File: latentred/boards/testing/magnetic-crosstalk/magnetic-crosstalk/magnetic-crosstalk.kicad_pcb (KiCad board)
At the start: 4 copper layers, 82.4 x 89 mm, 45 parts, among them J1 STEWART_SS_74500_024, J2 SMA, J3 SMA, J4 SMA, J5 SMA, J6 SMA, J7 SMA, J8 SMA, J9 SMA

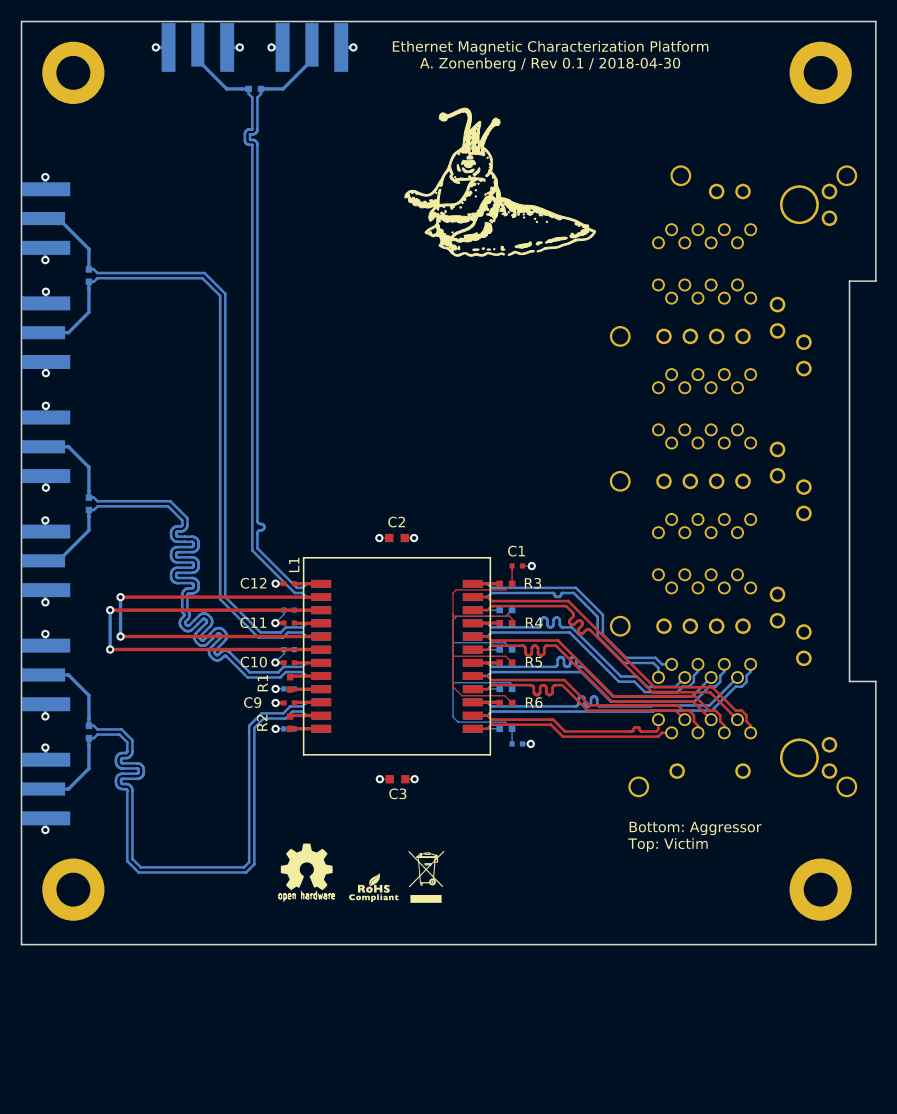
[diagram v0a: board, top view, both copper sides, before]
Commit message: Finished initial version of crosstalk characterization board
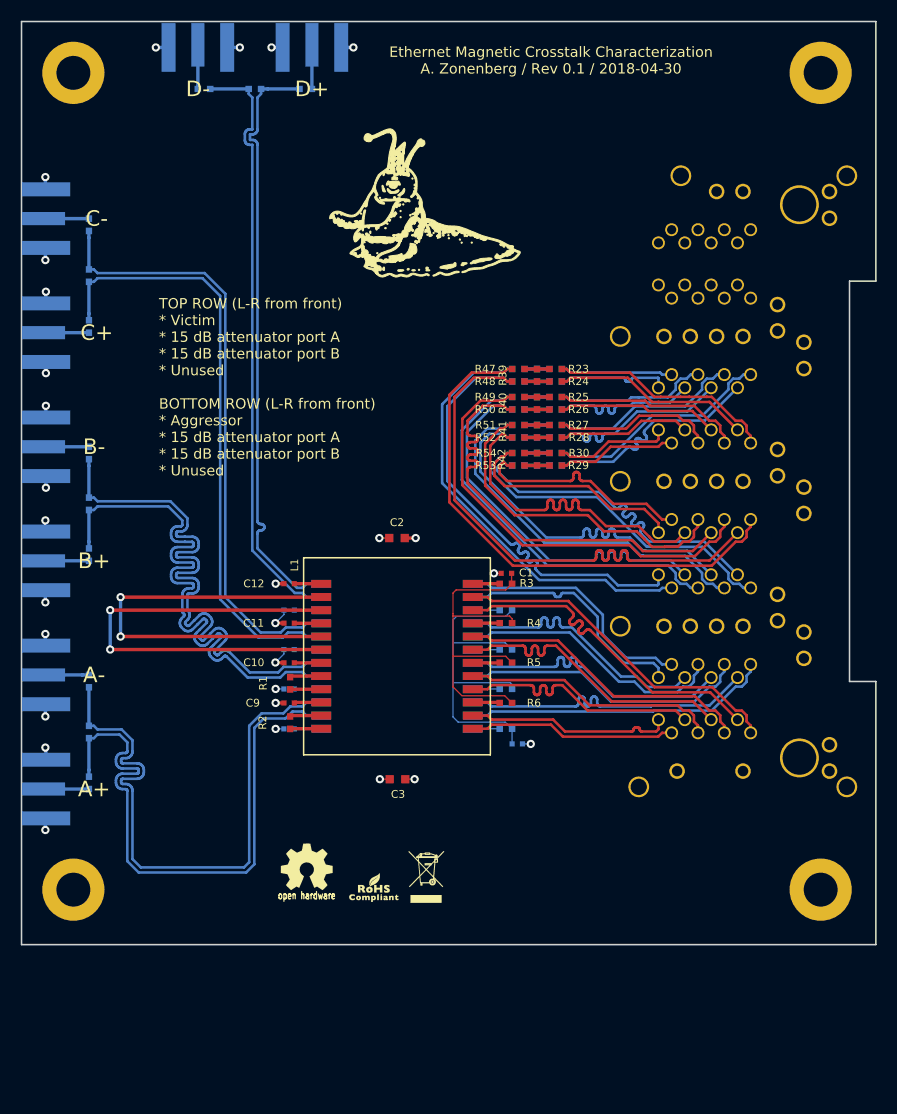
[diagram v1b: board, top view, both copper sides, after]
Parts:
- added R15: 953, azonenberg_pcb:EIA_0402_RES_NOSILK, B.Cu at (171.5, 94.4)
- added R16: 953, azonenberg_pcb:EIA_0402_RES_NOSILK, B.Cu at (171.5, 84.6)
- added R17: 953, azonenberg_pcb:EIA_0402_RES_NOSILK, B.Cu at (171.5, 72.4)
- added R18: 953, azonenberg_pcb:EIA_0402_RES_NOSILK, B.Cu at (171.5, 62.6)
- added R19: 953, azonenberg_pcb:EIA_0402_RES_NOSILK, B.Cu at (171.5, 50.4)
- added R20: 953, azonenberg_pcb:EIA_0402_RES_NOSILK, B.Cu at (171.5, 40.6)
- added R21: 953, azonenberg_pcb:EIA_0402_RES_NOSILK, B.Cu at (192.4, 27.5)
- added R22: 953, azonenberg_pcb:EIA_0402_RES_NOSILK, B.Cu at (182.6, 27.5)
- added R23: 34.8, azonenberg_pcb:EIA_0402_RES_NOSILK, F.Cu at (216.5, 54.5)
- added R24: 34.8, azonenberg_pcb:EIA_0402_RES_NOSILK, F.Cu at (216.5, 55.7)
- added R25: 34.8, azonenberg_pcb:EIA_0402_RES_NOSILK, F.Cu at (216.5, 57.2)
- added R26: 34.8, azonenberg_pcb:EIA_0402_RES_NOSILK, F.Cu at (216.5, 58.4)
- added R27: 34.8, azonenberg_pcb:EIA_0402_RES_NOSILK, F.Cu at (216.5, 59.9)
- added R28: 34.8, azonenberg_pcb:EIA_0402_RES_NOSILK, F.Cu at (216.5, 61.1)
- added R29: 34.8, azonenberg_pcb:EIA_0402_RES_NOSILK, F.Cu at (216.5, 63.8)
- added R30: 34.8, azonenberg_pcb:EIA_0402_RES_NOSILK, F.Cu at (216.5, 62.6)
- added R31: 34.8, azonenberg_pcb:EIA_0402_RES_NOSILK, B.Cu at (212.9, 62.6)
- added R32: 34.8, azonenberg_pcb:EIA_0402_RES_NOSILK, B.Cu at (212.9, 63.8)
- added R33: 34.8, azonenberg_pcb:EIA_0402_RES_NOSILK, B.Cu at (212.9, 59.9)
- added R34: 34.8, azonenberg_pcb:EIA_0402_RES_NOSILK, B.Cu at (212.9, 61.1)
- added R35: 34.8, azonenberg_pcb:EIA_0402_RES_NOSILK, B.Cu at (212.9, 57.2)
- added R36: 34.8, azonenberg_pcb:EIA_0402_RES_NOSILK, B.Cu at (212.9, 58.4)
- added R37: 34.8, azonenberg_pcb:EIA_0402_RES_NOSILK, B.Cu at (212.9, 54.5)
- added R38: 34.8, azonenberg_pcb:EIA_0402_RES_NOSILK, B.Cu at (212.9, 55.7)
- added R39: 36.5, azonenberg_pcb:EIA_0402_RES_NOSILK, F.Cu at (214.7, 55.1)
- added R40: 36.5, azonenberg_pcb:EIA_0402_RES_NOSILK, F.Cu at (214.7, 57.8)
- added R41: 36.5, azonenberg_pcb:EIA_0402_RES_NOSILK, F.Cu at (214.7, 60.5)
- added R42: 36.5, azonenberg_pcb:EIA_0402_RES_NOSILK, F.Cu at (214.7, 63.2)
- added R43: 36.5, azonenberg_pcb:EIA_0402_RES_NOSILK, B.Cu at (214.7, 63.2)
- added R44: 36.5, azonenberg_pcb:EIA_0402_RES_NOSILK, B.Cu at (214.7, 60.5)
- added R45: 36.5, azonenberg_pcb:EIA_0402_RES_NOSILK, B.Cu at (214.7, 57.8)
- added R46: 36.5, azonenberg_pcb:EIA_0402_RES_NOSILK, B.Cu at (214.7, 55.1)
- added R47: 34.8, azonenberg_pcb:EIA_0402_RES_NOSILK, F.Cu at (212.9, 54.5)
- added R48: 34.8, azonenberg_pcb:EIA_0402_RES_NOSILK, F.Cu at (212.9, 55.7)
- added R49: 34.8, azonenberg_pcb:EIA_0402_RES_NOSILK, F.Cu at (212.9, 57.2)
- added R50: 34.8, azonenberg_pcb:EIA_0402_RES_NOSILK, F.Cu at (212.9, 58.4)
- added R51: 34.8, azonenberg_pcb:EIA_0402_RES_NOSILK, F.Cu at (212.9, 59.9)
- added R52: 34.8, azonenberg_pcb:EIA_0402_RES_NOSILK, F.Cu at (212.9, 61.1)
- added R53: 34.8, azonenberg_pcb:EIA_0402_RES_NOSILK, F.Cu at (212.9, 63.8)
- added R54: 34.8, azonenberg_pcb:EIA_0402_RES_NOSILK, F.Cu at (212.9, 62.6)
- added R55: 34.8, azonenberg_pcb:EIA_0402_RES_NOSILK, B.Cu at (216.5, 62.6)
- added R56: 34.8, azonenberg_pcb:EIA_0402_RES_NOSILK, B.Cu at (216.5, 63.8)
- added R57: 34.8, azonenberg_pcb:EIA_0402_RES_NOSILK, B.Cu at (216.5, 59.9)
- added R58: 34.8, azonenberg_pcb:EIA_0402_RES_NOSILK, B.Cu at (216.5, 61.1)
- added R59: 34.8, azonenberg_pcb:EIA_0402_RES_NOSILK, B.Cu at (216.5, 57.2)
- added R60: 34.8, azonenberg_pcb:EIA_0402_RES_NOSILK, B.Cu at (216.5, 58.4)
- added R61: 34.8, azonenberg_pcb:EIA_0402_RES_NOSILK, B.Cu at (216.5, 54.5)
- added R62: 34.8, azonenberg_pcb:EIA_0402_RES_NOSILK, B.Cu at (216.5, 55.7)
- moved G*** 7.52 mm to (205.0, 39.2)
- moved C1 1.26 mm to (211.8, 74.2), turned to 0 degrees
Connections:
- J1 pad C1: (no net) -> /A2_A_P
- J1 pad C10: (no net) -> Net-(J1-PadC10)
- J1 pad C11: (no net) -> Net-(J1-PadC11)
- J1 pad C12: (no net) -> Net-(J1-PadC12)
- J1 pad C2: (no net) -> /A2_A_N
- J1 pad C3: (no net) -> /A2_B_P
- J1 pad C4: (no net) -> /A2_B_N
- J1 pad C5: (no net) -> /A2_C_P
- J1 pad C6: (no net) -> /A2_C_N
- J1 pad C7: (no net) -> /A2_D_P
- J1 pad C8: (no net) -> /A2_D_N
- J1 pad C9: (no net) -> Net-(J1-PadC9)
- J1 pad D1: (no net) -> /A1X_A_P
- J1 pad D10: (no net) -> Net-(J1-PadD10)
- J1 pad D11: (no net) -> Net-(J1-PadD11)
- J1 pad D12: (no net) -> Net-(J1-PadD12)
- J1 pad D2: (no net) -> /A1X_A_N
- J1 pad D3: (no net) -> /A1X_B_P
- J1 pad D4: (no net) -> /A1X_B_N
- J1 pad D5: (no net) -> /A1X_C_P
- J1 pad D6: (no net) -> /A1X_C_N
- J1 pad D7: (no net) -> /A1X_D_P
- J1 pad D8: (no net) -> /A1X_D_N
- J1 pad D9: (no net) -> Net-(J1-PadD9)
- J1 pad E1: (no net) -> /A1_A_P
- J1 pad E10: (no net) -> Net-(J1-PadE10)
- J1 pad E11: (no net) -> Net-(J1-PadE11)
- J1 pad E12: (no net) -> Net-(J1-PadE12)
- J1 pad E2: (no net) -> /A1_A_N
- J1 pad E3: (no net) -> /A1_B_P
- J1 pad E4: (no net) -> /A1_B_N
- J1 pad E5: (no net) -> /A1_C_P
- J1 pad E6: (no net) -> /A1_C_N
- J1 pad E7: (no net) -> /A1_D_P
- J1 pad E8: (no net) -> /A1_D_N
- J1 pad E9: (no net) -> Net-(J1-PadE9)
- J1 pad F1: (no net) -> /A2X_A_P
- J1 pad F10: (no net) -> Net-(J1-PadF10)
- J1 pad F11: (no net) -> Net-(J1-PadF11)
- J1 pad F12: (no net) -> Net-(J1-PadF12)
- J1 pad F2: (no net) -> /A2X_A_N
- J1 pad F3: (no net) -> /A2X_B_P
- J1 pad F4: (no net) -> /A2X_B_N
- J1 pad F5: (no net) -> /A2X_C_P
- J1 pad F6: (no net) -> /A2X_C_N
- J1 pad F7: (no net) -> /A2X_D_P
- J1 pad F8: (no net) -> /A2X_D_N
- J1 pad F9: (no net) -> Net-(J1-PadF9)
- J2 pad 1: /A_P -> Net-(J2-Pad1)
- J3 pad 1: /A_N -> Net-(J3-Pad1)
- J4 pad 1: /B_P -> Net-(J4-Pad1)
- J5 pad 1: /B_N -> Net-(J5-Pad1)
- J6 pad 1: /C_P -> Net-(J6-Pad1)
- J7 pad 1: /C_N -> Net-(J7-Pad1)
- J8 pad 1: /D_P -> Net-(J8-Pad1)
- J9 pad 1: /D_N -> Net-(J9-Pad1)
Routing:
- net /A1X_A_N: track 0.00 -> 51.6 mm
- net /A1X_A_P: track 0.00 -> 51.6 mm
- net /A1X_B_N: track 0.00 -> 42.4 mm
- net /A1X_B_P: track 0.00 -> 42.4 mm
- net /A2_D_N: track 0.00 -> 42.3 mm
- net /A2_D_P: track 0.00 -> 42.3 mm
- net /A2_C_N: track 0.00 -> 38.4 mm
- net /A2_C_P: track 0.00 -> 38.4 mm
- net /A2_B_N: track 0.00 -> 36.3 mm
- net /A2_B_P: track 0.00 -> 36.3 mm
- net /A2_A_N: track 0.00 -> 33.1 mm
- net /A2_A_P: track 0.00 -> 33.1 mm
- net /A1X_C_N: track 0.00 -> 32.2 mm
- net /A1X_C_P: track 0.00 -> 32.2 mm
- net /GND: track 192.7 -> 219.7 mm
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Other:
- board text added: "A+"
- board text added: "A-"
- board text added: "B+"
- board text added: "B-"
- board text added: "C+"
- board text added: "C-"
- board text added: "D+"
- board text added: "D-"
- board text added: "Ethernet Magnetic Crosstalk Characterization A. Zonenberg / Rev 0.1 / 2018-04-30"
- board text added: "TOP ROW (L-R from front) * Victim * 15 dB attenuator port A * 15 dB attenuator port B * Unused BOTTOM ROW (L-R from front) * Aggressor * 15 dB attenuator port A * 15 dB attenuator port B * Unused"
- board text removed: "Bottom: Aggressor Top: Victim"
- board text removed: "Ethernet Magnetic Characterization Platform A. Zonenberg / Rev 0.1 / 2018-04-30"

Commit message: Began updating magnetic-crosstalk board for v0.2
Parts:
- moved L1 39.9 mm to (228.0, 111.8)
- moved L2 34.8 mm to (201.8, 117.0)
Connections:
- L1 pad 1: Net-(C12-Pad2) -> Net-(L1-Pad1)
- L1 pad 10: Net-(C9-Pad2) -> Net-(L1-Pad10)
- L1 pad 11: Net-(L1-Pad11) -> /AGG_D_N
- L1 pad 12: Net-(L1-Pad12) -> /AGG_D_P
- L1 pad 13: /AGG_D_P -> Net-(L1-Pad13)
- L1 pad 14: /AGG_D_N -> Net-(L1-Pad14)
- L1 pad 15: Net-(L1-Pad15) -> Net-(C9-Pad2)
- L1 pad 16: /AGG_C_N -> Net-(L1-Pad16)
- L1 pad 17: /AGG_C_P -> Net-(L1-Pad17)
- L1 pad 18: Net-(L1-Pad18) -> Net-(C10-Pad2)
- L1 pad 19: /AGG_B_N -> Net-(L1-Pad19)
- L1 pad 2: Net-(L1-Pad2) -> /AGG_A_P
- L1 pad 20: /AGG_B_P -> Net-(L1-Pad20)
- L1 pad 21: Net-(L1-Pad21) -> Net-(C11-Pad2)
- L1 pad 22: /AGG_A_N -> Net-(L1-Pad19)
- L1 pad 23: /AGG_A_P -> Net-(L1-Pad20)
- L1 pad 24: Net-(L1-Pad24) -> Net-(C12-Pad2)
- L1 pad 3: Net-(L1-Pad3) -> /AGG_A_N
- L1 pad 4: Net-(C11-Pad2) -> Net-(L1-Pad4)
- L1 pad 5: Net-(L1-Pad2) -> /AGG_B_P
- L1 pad 6: Net-(L1-Pad3) -> /AGG_B_N
- L1 pad 7: Net-(C10-Pad2) -> Net-(L1-Pad7)
- L1 pad 8: Net-(L1-Pad8) -> /AGG_C_P
- L1 pad 9: Net-(L1-Pad9) -> /AGG_C_N
- L2 pad 1: Net-(C7-Pad2) -> Net-(L2-Pad1)
- L2 pad 10: Net-(C4-Pad2) -> Net-(L2-Pad10)
- L2 pad 11: /D_N -> /VIC_D_N
- L2 pad 12: /D_P -> /VIC_D_P
- L2 pad 13: /VIC_D_P -> /D_P
- L2 pad 14: /VIC_D_N -> /D_N
- L2 pad 15: Net-(L2-Pad15) -> Net-(C4-Pad2)
- L2 pad 16: /VIC_C_N -> /C_N
- L2 pad 17: /VIC_C_P -> /C_P
- L2 pad 18: Net-(L2-Pad18) -> Net-(C5-Pad2)
- L2 pad 19: /VIC_B_N -> /B_N
- L2 pad 2: /A_P -> /VIC_A_P
- L2 pad 20: /VIC_B_P -> /B_P
- L2 pad 21: Net-(L2-Pad21) -> Net-(C6-Pad2)
- L2 pad 22: /VIC_A_N -> /A_N
- L2 pad 23: /VIC_A_P -> /A_P
- L2 pad 24: Net-(L2-Pad24) -> Net-(C7-Pad2)
- L2 pad 3: /A_N -> /VIC_A_N
- L2 pad 4: Net-(C6-Pad2) -> Net-(L2-Pad4)
- L2 pad 5: /B_P -> /VIC_B_P
- L2 pad 6: /B_N -> /VIC_B_N
- L2 pad 7: Net-(C5-Pad2) -> Net-(L2-Pad7)
- L2 pad 8: /C_P -> /VIC_C_P
- L2 pad 9: /C_N -> /VIC_C_N
- R1 pad 1: Net-(L1-Pad8) -> Net-(L1-Pad17)
- R1 pad 2: Net-(L1-Pad9) -> Net-(L1-Pad16)
- R11 pad 2: Net-(L2-Pad24) -> Net-(L2-Pad1)
- R12 pad 2: Net-(L2-Pad21) -> Net-(L2-Pad4)
- R13 pad 2: Net-(L2-Pad18) -> Net-(L2-Pad7)
- R14 pad 2: Net-(L2-Pad15) -> Net-(L2-Pad10)
- R2 pad 1: Net-(L1-Pad11) -> Net-(L1-Pad14)
- R2 pad 2: Net-(L1-Pad12) -> Net-(L1-Pad13)
- R3 pad 2: Net-(L1-Pad24) -> Net-(L1-Pad1)
- R4 pad 2: Net-(L1-Pad21) -> Net-(L1-Pad4)
- R5 pad 2: Net-(L1-Pad18) -> Net-(L1-Pad7)
- R6 pad 2: Net-(L1-Pad15) -> Net-(L1-Pad10)
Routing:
- net Net-(L1-Pad3): track 44.5 -> 0.00 mm, vias 2 -> 0
- net Net-(L1-Pad2): track 42.5 -> 0.00 mm, vias 2 -> 0
- net Net-(L1-Pad8): track 3.04 -> 0.00 mm
- net Net-(L1-Pad11): track 3.04 -> 0.00 mm
- net Net-(L1-Pad9): track 3.01 -> 0.00 mm
- net Net-(L1-Pad12): track 3.01 -> 0.00 mm
- net Net-(L1-Pad15): track 2.63 -> 0.00 mm
- net Net-(L1-Pad18): track 2.62 -> 0.00 mm
- net Net-(L2-Pad21): track 2.62 -> 0.00 mm
- net Net-(L1-Pad21): track 2.62 -> 0.00 mm
- net Net-(L1-Pad24): track 2.61 -> 0.00 mm
- net Net-(C6-Pad2): track 2.61 -> 0.00 mm
- net Net-(L2-Pad24): track 2.61 -> 0.00 mm
- net Net-(L2-Pad18): track 2.61 -> 0.00 mm
- net Net-(C12-Pad2): track 2.61 -> 0.00 mm
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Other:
- board text added: "Ethernet Magnetic Crosstalk Characterization A. Zonenberg / Rev 0.2 / 2018-05-14"
- board text removed: "Ethernet Magnetic Crosstalk Characterization A. Zonenberg / Rev 0.1 / 2018-04-30"
